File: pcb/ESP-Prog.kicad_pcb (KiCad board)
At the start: 2 copper layers, 60 x 25 mm, 71 parts, among them IC1 M93C46-WMN6TP, IC2 MC74VHC1GT04DFT1, IC3 74AHC125BQ,115, J1 UJ2-MIBH-G-SMT-TR, J2 Conn_01x03, J3 Conn_02x05_Odd_Even, J4 Conn_01x03, J5 Conn_01x03, J6 Conn_02x03_Odd_Even, Q1 MMSS8050-H-TP, Q2 MMSS8050-H-TP, Q3 AO3401A, U1 LD1117S33TR_SOT223, U2 FT2232HL, Y1 ECS-120-18-33-JEM-TR

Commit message: probando de commitear con token
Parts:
- removed IC1: M93C46-WMN6TP, SamacSys_Parts:SOIC127P600X175-8N
- removed IC2: MC74VHC1GT04DFT1, SamacSys_Parts:SOT65P210X110-5N
- removed IC3: 74AHC125BQ,115, SamacSys_Parts:QFN50P250X300X100-15N-D
- added U3: M93C46-WMN6TP, SamacSys_Parts:SOIC127P600X175-8N, F.Cu at (137.0, 103.0)
- added U4: MC74VHC1GT04DFT1, SamacSys_Parts:SOT65P210X110-5N, F.Cu at (139.0, 114.0)
- added U5: 74AHC125BQ,115, SamacSys_Parts:QFN50P250X300X100-15N-D, F.Cu at (137.5, 122.5)
- moved D9 62.5 mm to (108.8, 114.8), turned to 270 degrees
- moved D1 45.7 mm to (109.5, 111.2), turned to 180 degrees
- moved D8 44.6 mm to (113.8, 107.0)
- moved D7 43.9 mm to (113.8, 109.5)
- moved J2 5.10 mm to (148.0, 117.0)
- moved Q2 3.04 mm to (97.5, 63.0)
- moved U1 1.27 mm to (114.8, 120.2)
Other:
- board text added: "Grilla 1: 0.5mm Grilla 2: 0.25mm"

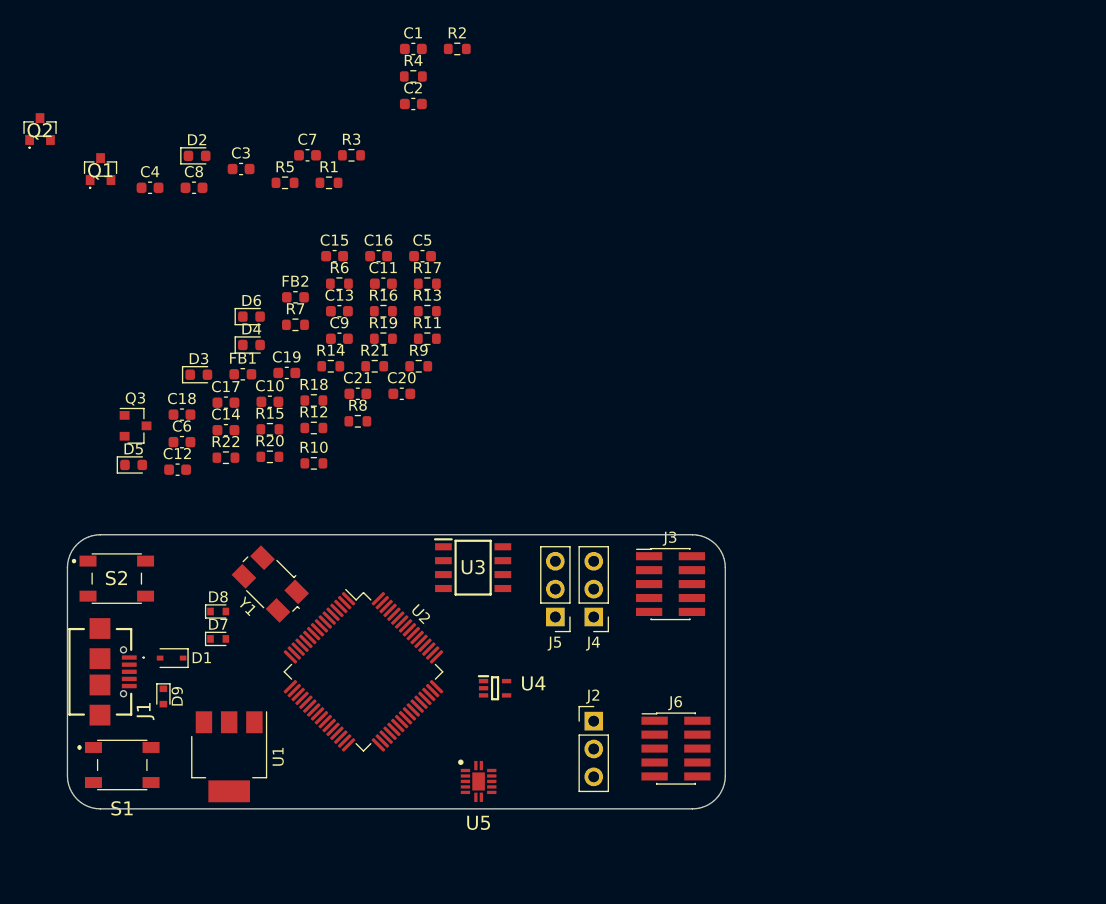
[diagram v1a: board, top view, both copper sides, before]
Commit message: correcciones al esquematico y avances en posicionamiento de pcb
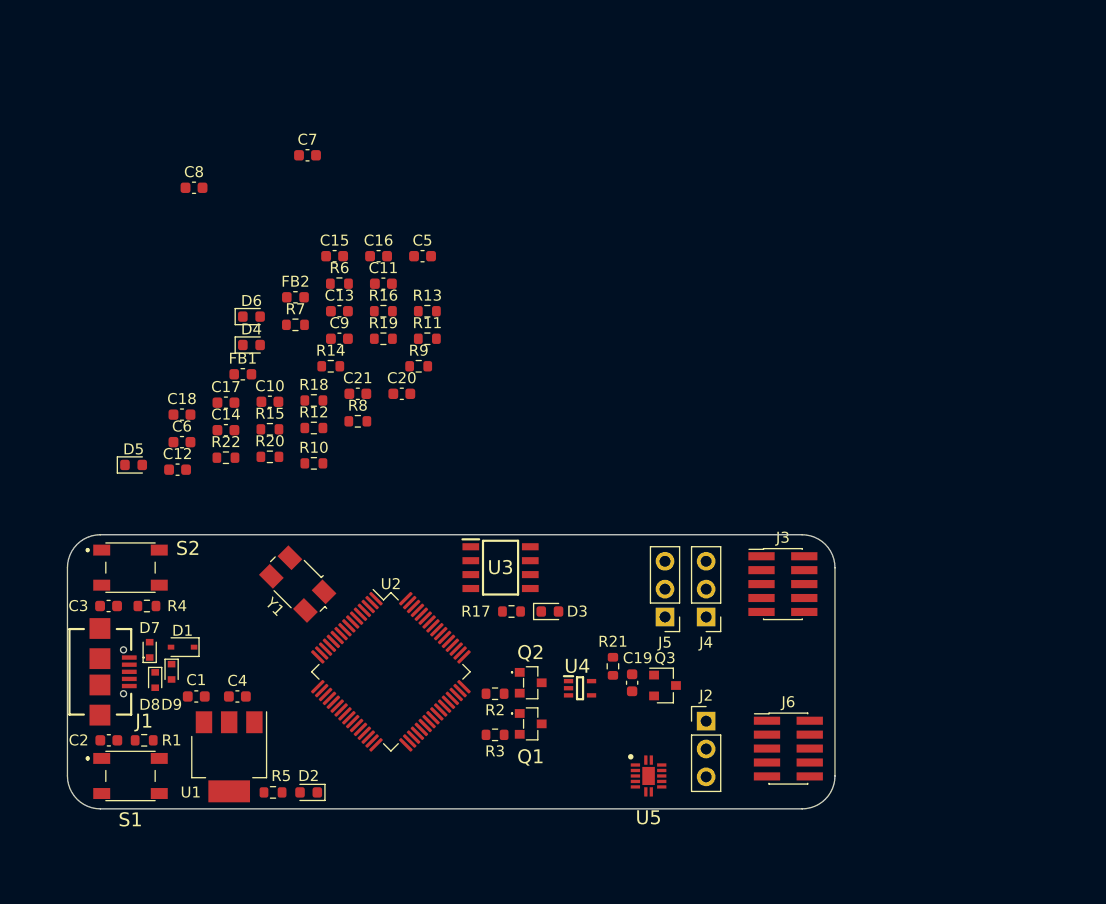
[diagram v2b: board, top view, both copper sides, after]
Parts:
- R5: value R -> 2k2
- moved Q2 67.5 mm to (142.2, 113.5), turned to 270 degrees
- moved C2 64.3 mm to (103.8, 118.8), turned to 180 degrees
- moved Q1 64.0 mm to (142.2, 117.2), turned to 270 degrees
- moved C1 62.3 mm to (111.8, 114.8), turned to 180 degrees
- moved D2 58.9 mm to (122.0, 123.5), turned to 180 degrees
- moved R2 58.9 mm to (139.0, 114.5)
- moved R5 55.6 mm to (118.8, 123.5), turned to 180 degrees
- moved R3 54.5 mm to (139.0, 118.2)
- moved R4 54.1 mm to (107.2, 106.5), turned to 180 degrees
- moved Q3 53.8 mm to (154.5, 113.8)
- moved R1 53.6 mm to (107.0, 118.8), turned to 180 degrees
- moved C4 47.1 mm to (115.5, 114.8)
- moved C19 42.3 mm to (151.5, 113.5), turned to 90 degrees
- moved C3 41.6 mm to (103.8, 106.5), turned to 180 degrees
- moved D3 38.6 mm to (144.0, 107.0)
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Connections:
- S2 pad 4: Net-(S2-Pad4) -> /ESP_IO0_B
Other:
- board size 60 x 25 mm -> 70 x 25 mm

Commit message: - Rpimer propuesta posicionamiento
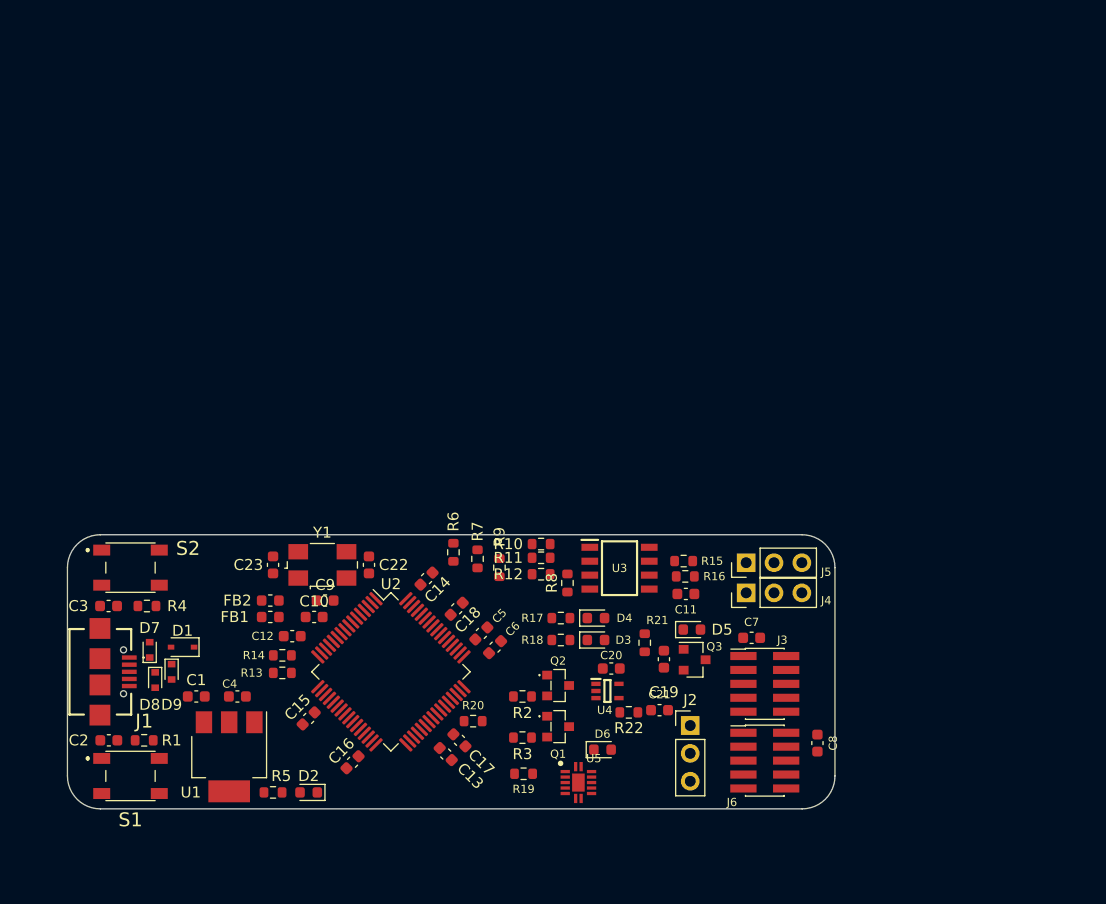
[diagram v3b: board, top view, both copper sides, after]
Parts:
- added C22: 12pF 5%, Capacitor_SMD:C_0603_1608Metric, F.Cu at (127.5, 102.8)
- added C23: 12pF 5%, Capacitor_SMD:C_0603_1608Metric, F.Cu at (118.8, 102.8)
- moved C8 76.1 mm to (168.4, 119.0), turned to 270 degrees
- moved C7 59.8 mm to (162.4, 109.4)
- moved D5 53.1 mm to (156.9, 108.7)
- moved D6 50.8 mm to (148.8, 119.6)
- moved C16 46.2 mm to (126.0, 120.8), turned to 45 degrees
- moved R22 43.5 mm to (151.2, 116.2), turned to 180 degrees
- moved C15 42.2 mm to (122.0, 116.8), turned to 45 degrees
- moved R19 41.7 mm to (141.6, 121.8)
- moved C13 41.5 mm to (134.5, 120.0), turned to 135 degrees
- moved D4 40.1 mm to (148.2, 107.6)
- moved C21 39.9 mm to (154.0, 116.0)
- moved R15 39.6 mm to (156.2, 102.4), turned to 180 degrees
- moved C11 39.5 mm to (156.4, 105.4), turned to 180 degrees
- moved C17 37.4 mm to (135.8, 118.8), turned to 135 degrees
- moved R16 36.6 mm to (156.3, 103.8), turned to 180 degrees
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
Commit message: - Se modifica el esquemático para respetar la estructura gerarquica
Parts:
- R1, R4: value R -> 10k
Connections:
- net /ESP_IO0 renamed /conectores_fuente/ESP_IO0
- net /ESP_IO0_B renamed /conectores_fuente/ESP_IO0_B
- net ESP_EN renamed /conectores_fuente/ESP_EN
- net ESP_RXD0 renamed /conectores_fuente/ESP_RXD0
- net ESP_TCK renamed /conectores_fuente/ESP_TCK
- net ESP_TDI renamed /conectores_fuente/ESP_TDI
- net ESP_TDO renamed /conectores_fuente/ESP_TDO
- net ESP_TMS renamed /conectores_fuente/ESP_TMS
- net ESP_TXD0 renamed /conectores_fuente/ESP_TXD0
- net FT_nDTR renamed /conectores_fuente/FT_nDTR
- net FT_nRTS renamed /conectores_fuente/FT_nRTS
- net USB_DM renamed /conectores_fuente/USB_DM
- net USB_DP renamed /conectores_fuente/USB_DP

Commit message: avances en el pcb y correcciones al esquematico
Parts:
- J6: footprint Connector_PinHeader_1.27mm:PinHeader_2x05_P1.27mm_Vertical_SMD -> Connector_PinHeader_1.27mm:PinHeader_2x03_P1.27mm_Vertical_SMD
- moved D5 36.6 mm to (125.2, 126.8), turned to 180 degrees
- moved C7 32.3 mm to (190.7, 125.0), turned to 180 degrees
- moved C19 31.3 mm to (127.7, 127.6)
- moved Q3 31.1 mm to (130.5, 127.4)
- moved R20 27.9 mm to (164.9, 118.0)
- moved R21 26.9 mm to (130.3, 124.8), turned to 180 degrees
- moved J3 26.9 mm to (189.6, 120.3), turned to 180 degrees
- moved R19 20.6 mm to (161.8, 117.9), turned to 270 degrees
- moved R13 14.0 mm to (131.5, 105.2), turned to 45 degrees
- moved D6 12.3 mm to (161.0, 121.4)
- moved R10 11.5 mm to (134.0, 107.8), turned to 45 degrees
- moved R11 9.92 mm to (135.7, 108.6), turned to 45 degrees
- moved C23 9.44 mm to (127.9, 105.3), turned to 135 degrees
- moved R6 8.56 mm to (143.8, 102.0)
- moved C9 7.31 mm to (116.2, 105.6), turned to 90 degrees
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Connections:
- C12 pad 2: Net-(C12-Pad2) -> +1V8
- C13 pad 2: Net-(C13-Pad2) -> +1V8
- C14 pad 2: Net-(C14-Pad2) -> +1V8
- C15 pad 2: Net-(C15-Pad2) -> +3V3
- C16 pad 2: Net-(C16-Pad2) -> +3V3
- C17 pad 2: Net-(C17-Pad2) -> +3V3
- C18 pad 2: Net-(C18-Pad2) -> +3V3
- U2 pad 12: Net-(C12-Pad2) -> +1V8
- U2 pad 20: Net-(C15-Pad2) -> +3V3
- U2 pad 31: Net-(C16-Pad2) -> +3V3
- U2 pad 37: Net-(C13-Pad2) -> +1V8
- U2 pad 42: Net-(C17-Pad2) -> +3V3
- U2 pad 56: Net-(C18-Pad2) -> +3V3
- U2 pad 64: Net-(C14-Pad2) -> +1V8
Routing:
- net +3V3: track 0.00 -> 163.4 mm, vias 0 -> 2
- net +5V: track 0.00 -> 71.6 mm, vias 0 -> 1
- net /conectores_fuente/ESP_EN: track 0.00 -> 62.6 mm, vias 0 -> 2
- net /conectores_fuente/ESP_IO0_B: track 0.00 -> 61.8 mm, vias 0 -> 2
- net +1V8: track 0.00 -> 38.9 mm, vias 0 -> 4
- net /conectores_fuente/USB_DM: track 0.00 -> 23.7 mm
- net /conectores_fuente/USB_DP: track 0.00 -> 22.9 mm
- net Net-(C9-Pad1): track 0.00 -> 20.1 mm, vias 0 -> 2
- net /conectores_fuente/FT_nRTS: track 0.00 -> 18.7 mm
- net Net-(C10-Pad1): track 0.00 -> 18.6 mm, vias 0 -> 2
- net /ftdi/EECS: track 0.00 -> 17.3 mm
- net /ftdi/EECLK: track 0.00 -> 15.2 mm, vias 0 -> 2
- net Net-(R12-Pad1): track 0.00 -> 14.8 mm, vias 0 -> 2
- net /conectores_fuente/FT_nDTR: track 0.00 -> 14.7 mm
- net Net-(R18-Pad2): track 0.00 -> 14.2 mm, vias 0 -> 2
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- added copper zone on F.Cu, net +3V3
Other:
- board size 70 x 25 mm -> 70 x 30 mm
- net class Default: trace_width 0.25 -> 0.2
- net class power added: clearance 0.2, trace_width 0.4, via_dia 0.8, via_drill 0.4

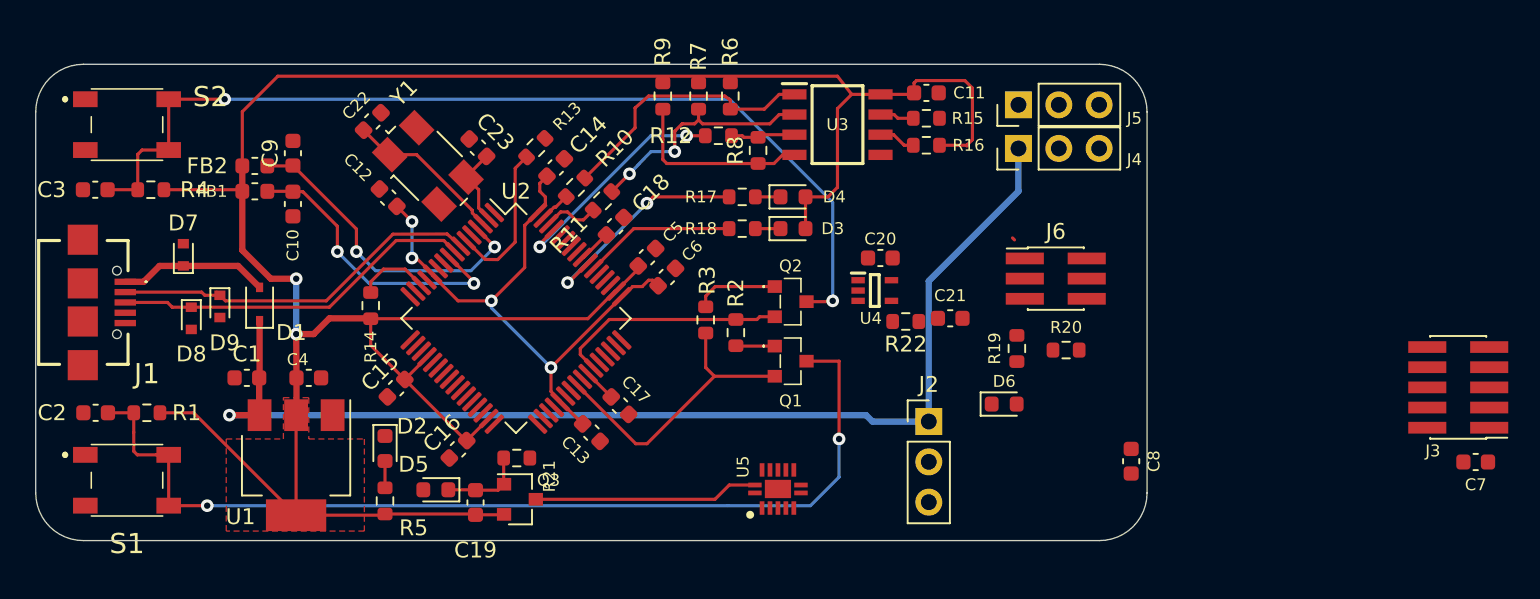
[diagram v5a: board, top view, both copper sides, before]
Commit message: Primer versión ruteo terminada
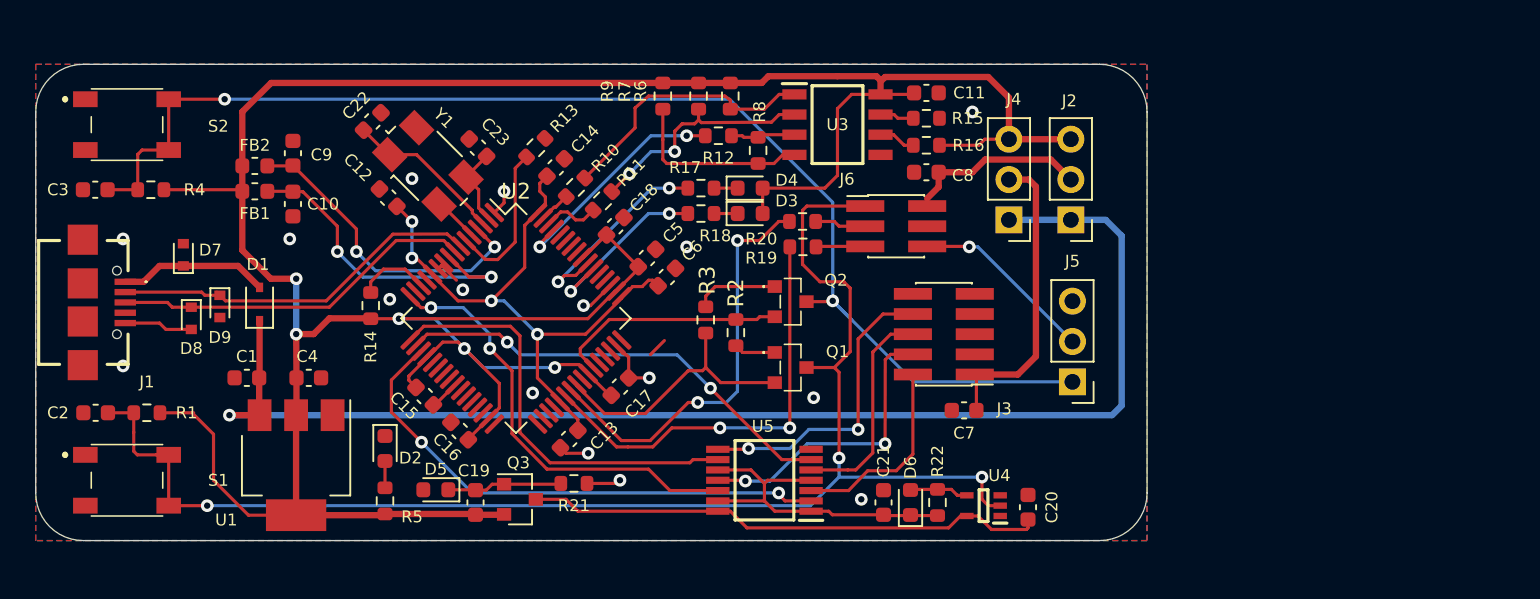
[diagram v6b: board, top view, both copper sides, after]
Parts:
- U5: value 74AHC125BQ,115 -> 74AHC125PW-Q100,11; footprint SamacSys_Parts:QFN50P250X300X100-15N-D -> SamacSys_Parts:SOP65P640X110-14N
- moved J3 32.6 mm to (157.2, 117.0)
- moved C7 32.4 mm to (158.5, 121.8)
- moved C8 22.3 mm to (156.1, 106.8), turned to 180 degrees
- moved R20 18.5 mm to (148.3, 109.9), turned to 180 degrees
- moved C20 18.2 mm to (162.5, 127.9), turned to 90 degrees
- moved J5 17.8 mm to (165.3, 120.0), turned to 180 degrees
- moved J2 15.5 mm to (165.2, 109.8), turned to 180 degrees
- moved U4 15.2 mm to (159.7, 127.8), turned to 180 degrees
- moved R19 14.9 mm to (148.3, 111.5), turned to 180 degrees
- moved C21 12.3 mm to (153.4, 127.6), turned to 90 degrees
- moved R22 11.6 mm to (156.8, 127.6), turned to 90 degrees
- moved J6 10.6 mm to (154.2, 110.2)
- moved D6 8.56 mm to (155.1, 127.6), turned to 90 degrees
- moved J4 4.54 mm to (161.3, 109.8), turned to 180 degrees
- moved R21 3.94 mm to (133.9, 126.4)
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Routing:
- net /ftdi/FT_TMS: track 0.00 -> 33.5 mm, vias 0 -> 2
- net +3V3: track 163.4 -> 194.1 mm, vias 2 -> 5
- net /ftdi/FT_TDO: track 0.00 -> 28.5 mm, vias 0 -> 2
- net /conectores_fuente/ESP_EN: track 62.6 -> 90.3 mm, vias 2 -> 3
- net Net-(R19-Pad2): track 0.00 -> 27.3 mm, vias 0 -> 2
- net /ftdi/FT_TCK: track 0.00 -> 27.3 mm, vias 0 -> 2
- net /ftdi/FT_TDI: track 0.00 -> 27.0 mm
- net Net-(R20-Pad2): track 0.00 -> 26.3 mm, vias 0 -> 2
- net GND: track 0.00 -> 24.0 mm, vias 0 -> 16
- net /ftdi/ESP_EN_N: track 0.00 -> 21.7 mm
- net VDDA: track 0.00 -> 19.3 mm
- net /conectores_fuente/ESP_TDI: track 0.00 -> 19.2 mm, vias 0 -> 2
- net /conectores_fuente/ESP_IO0_B: track 61.8 -> 80.7 mm
- net +3.3VP: track 14.2 -> 33.0 mm
- net /conectores_fuente/ESP_TCK: track 0.00 -> 18.7 mm, vias 0 -> 2
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- added copper zone on B.Cu, net GND
- added copper zone on F.Cu, net GND
- removed copper zone on F.Cu, net +3V3
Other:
- board text added: "Grilla 1: 0.5mm (bordes PCB) Grilla 2: 0.25mm (posicionamiento componentes) Grilla 3: 0.1mm (ruteo de pistas)"
- board text removed: "Grilla 1: 0.5mm Grilla 2: 0.25mm"

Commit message: revisiones
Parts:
- added FID1: Fiducial, Fiducial:Fiducial_0.5mm_Mask1mm, F.Cu at (167.0, 102.5)
- added FID2: Fiducial, Fiducial:Fiducial_0.5mm_Mask1mm, F.Cu at (161.0, 124.0)
- added FID3: Fiducial, Fiducial:Fiducial_0.5mm_Mask1mm, F.Cu at (108.5, 119.0)
- added H1: MountingHole, MountingHole:MountingHole_2.5mm, F.Cu at (166.5, 126.5)
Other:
- board text added: "3v3"
- board text added: "5v"
- board text added: "Grilla 1: 0.5mm (bordes PCB) Grilla 2: 0.25mm (posicionamiento componentes) Grilla 3: 0.1mm (ruteo de pistas) Pistas señal 0.2mm Pistas alimentación 0.4mm Clearence general 0.2mm Clearence fill: 0.4mm"
- board text removed: "Grilla 1: 0.5mm (bordes PCB) Grilla 2: 0.25mm (posicionamiento componentes) Grilla 3: 0.1mm (ruteo de pistas)"
